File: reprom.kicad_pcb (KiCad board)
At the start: 2 copper layers, 54.4 x 40.6 mm, 20 parts, among them P1 KERNAL_SOCKET, P10 NEW_LEFT, P11 SX64_RIGHT, P12 ANCIENT_RIGHT, P13 GND, P2 KERNAL_AND_BASIC_SOCKET, P3 ANCIENT_LEFT, P4 OLD_RIGHT, P5 KERNAL, P6 CHARSET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

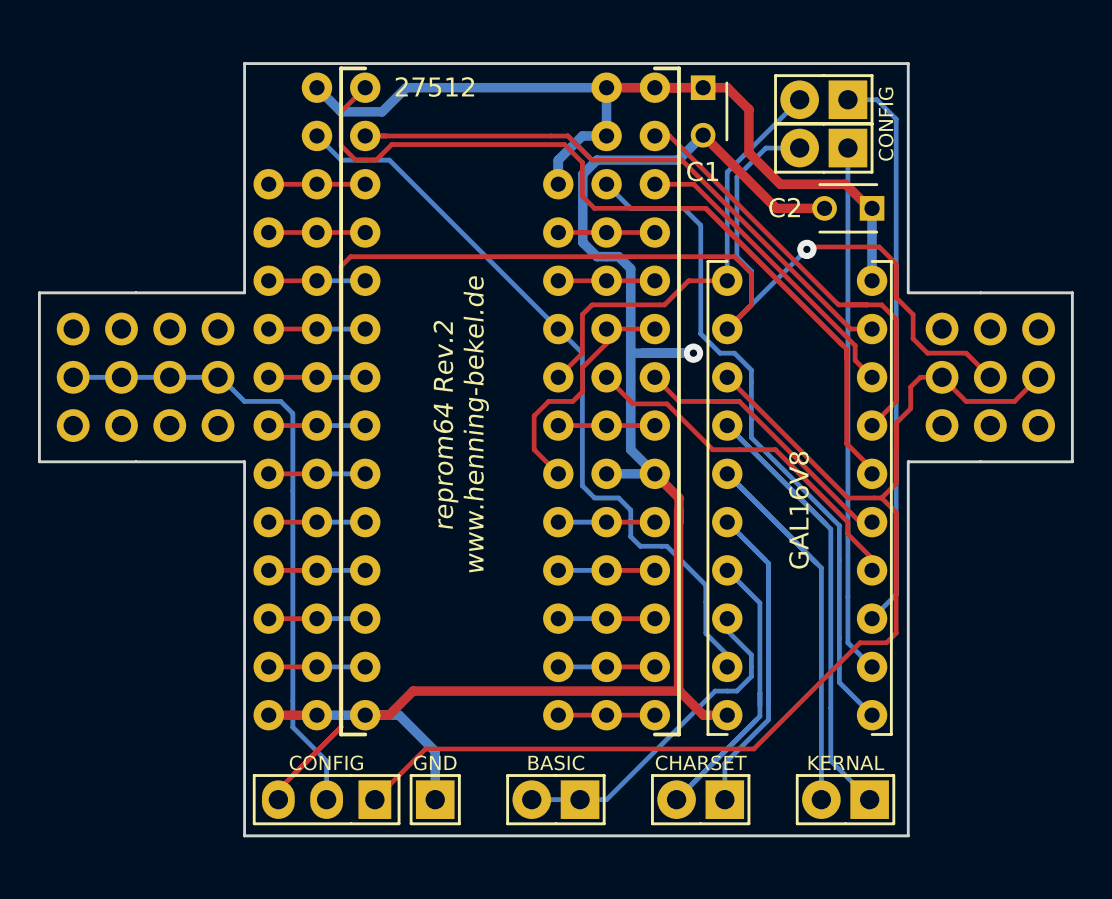
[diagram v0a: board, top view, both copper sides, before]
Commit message: Hardware: Added additional pin header for A5 and A8, rounded corners
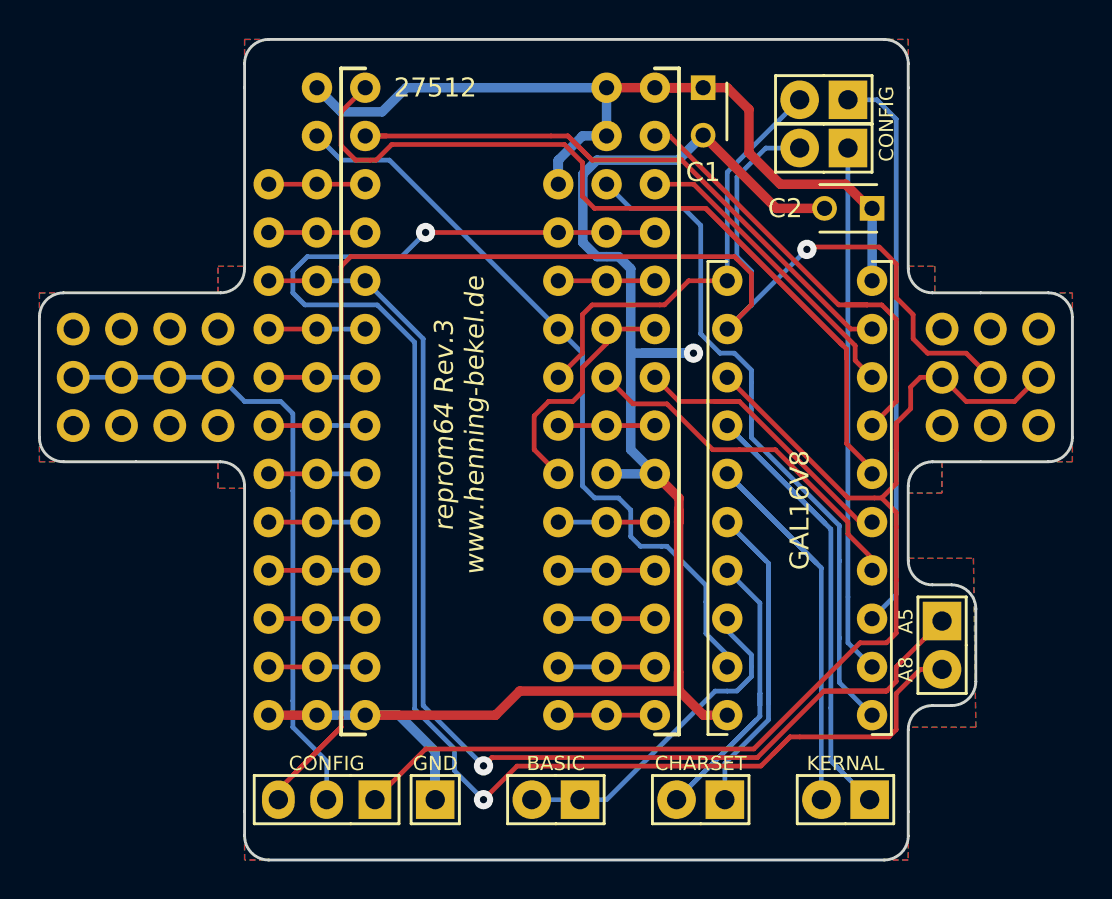
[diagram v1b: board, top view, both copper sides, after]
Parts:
- added P14: AUX, custom:Pin_Header_Straight_1x02, F.Cu at (158.8, 106.8)
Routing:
- net /A8: track 5.08 -> 83.4 mm, vias 0 -> 2
- net /A5: track 5.08 -> 64.2 mm, vias 0 -> 1
- net GND: track 86.5 -> 89.3 mm
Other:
- board size 54.4 x 40.6 mm -> 54.4 x 43.2 mm
- board text added: "A5"
- board text added: "A8"
- board text added: "reprom64 Rev.3 www.henning-bekel.de"
- board text removed: "reprom64 Rev.2 www.henning-bekel.de"

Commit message: Hardware: Moved A5 and A8 header to a more convenient location
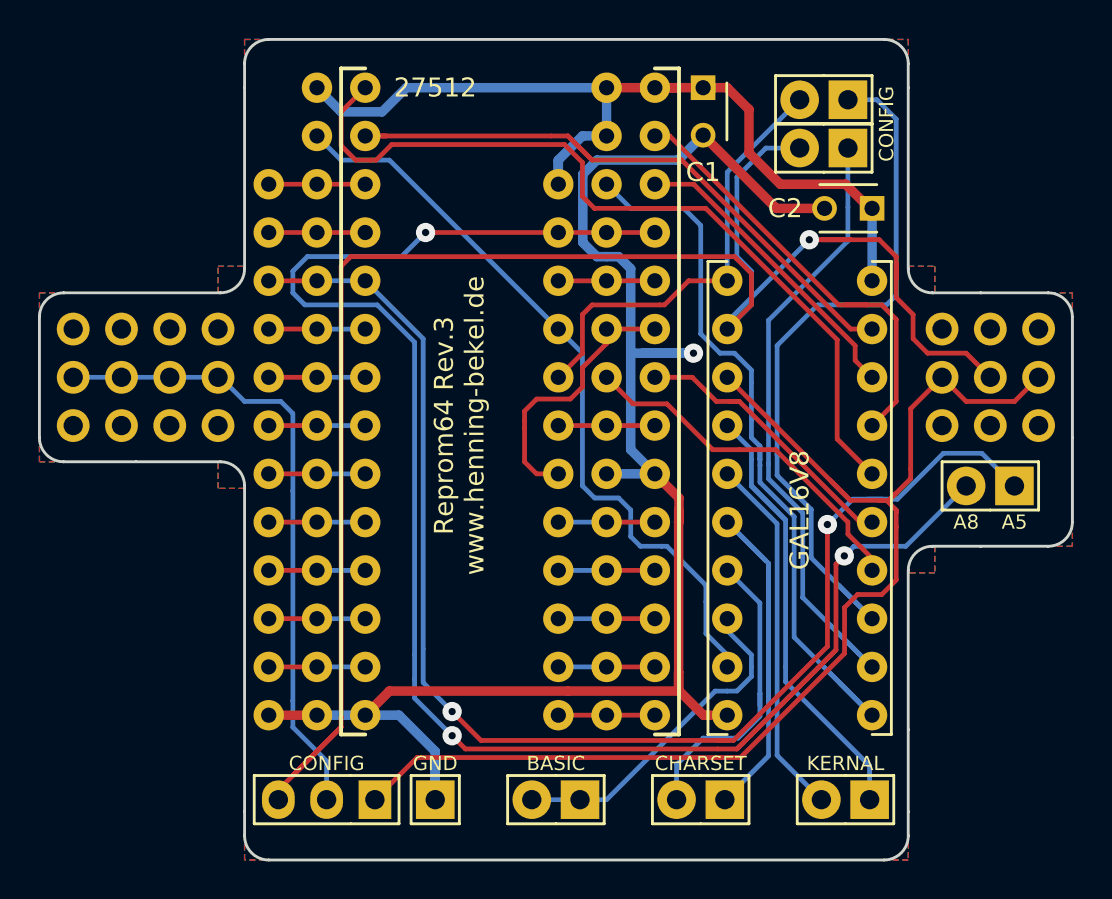
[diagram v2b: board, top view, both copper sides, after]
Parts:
- moved P14 8.07 mm to (162.6, 99.7), turned to 270 degrees
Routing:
- net /K1: track 31.2 -> 19.2 mm
- net /A15: track 54.1 -> 43.7 mm
- net /A8: track 83.4 -> 93.2 mm, vias 2 -> 3
- net /CKS: track 29.8 -> 38.5 mm
- net /A5: track 64.2 -> 72.0 mm, vias 1 -> 2
- net /BA14: track 35.8 -> 42.7 mm
- net /CBS: track 27.8 -> 34.4 mm
- net /C1: track 21.2 -> 16.3 mm
- net /K0: track 30.1 -> 25.4 mm
- net /BS: track 91.7 -> 95.0 mm
- net /A11: track 13.0 -> 14.4 mm
- net /OE: track 16.0 -> 15.2 mm
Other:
- outline, holes or cut-outs redrawn
- board text added: "Reprom64 Rev.3 www.henning-bekel.de"
- board text removed: "reprom64 Rev.3 www.henning-bekel.de"

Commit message: Hardware: Improved silkscreen, routing
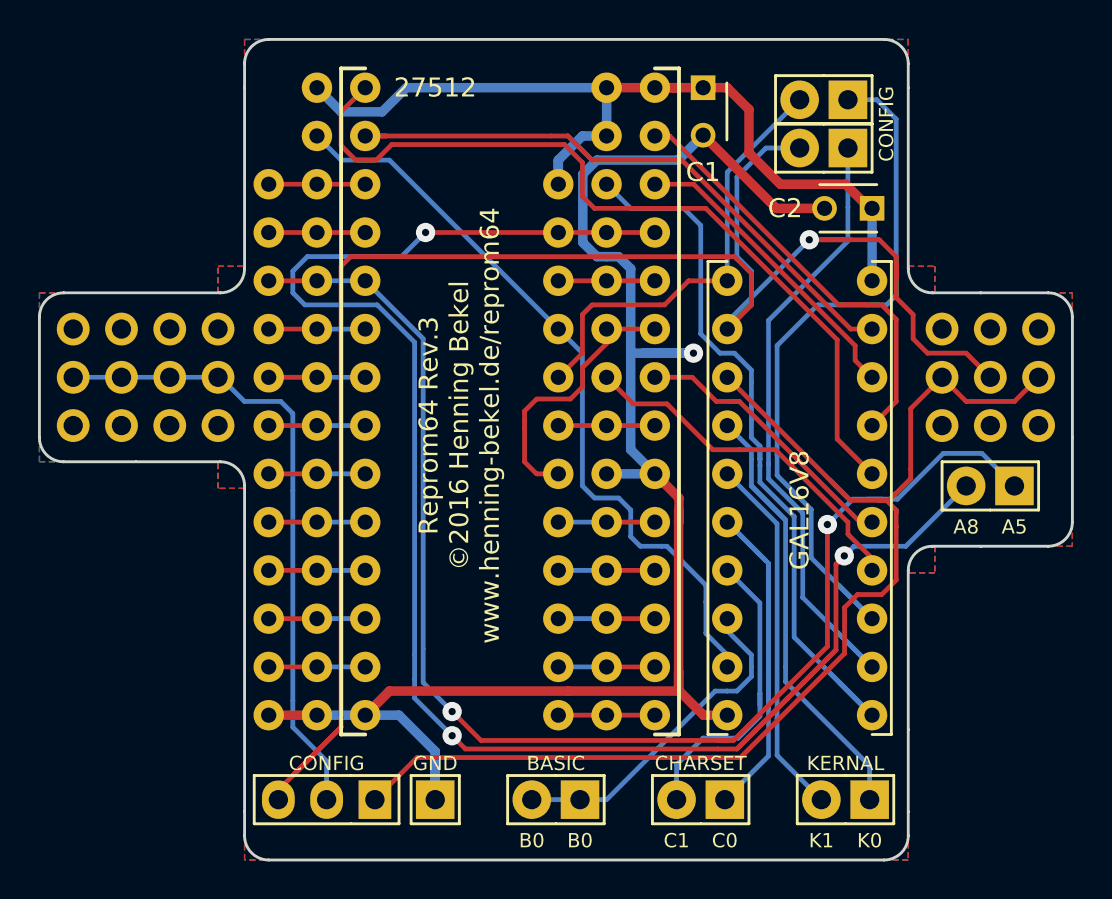
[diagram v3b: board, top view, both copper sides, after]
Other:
- board text added: "B0"
- board text added: "C0"
- board text added: "C1"
- board text added: "K0"
- board text added: "K1"
- board text added: "Reprom64 Rev.3 ©2016 Henning Bekel www.henning-bekel.de/reprom64"
- board text removed: "Reprom64 Rev.3 www.henning-bekel.de"
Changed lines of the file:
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@@
     (area 111.176999 76.124999 165.683001 119.455001)
     (thickness 1.6)
-    (drawings 50)
+    (drawings 56)
     (tracks 387)
     (zones 0)
@@
     (pad 2 thru_hole oval (at 0 2.54 270) (size 2.032 2.032) (drill 1.016) (layers *.Cu *.Mask F.SilkS)
       (net 24 /A8))
-    (model Pin_Headers.3dshapes/Pin_Header_Angled_1x02.wrl
-      (at (xyz 0 -0.05 0))
-      (scale (xyz 1 1 1))
-      (rotate (xyz 0 0 90))
-    )
+  )
+  (gr_text K0 (at 154.94 118.364) (layer F.SilkS)
+    (effects (font (size 0.75 0.75) (thickness 0.15)))
+  )
+  (gr_text K1 (at 152.4 118.364) (layer F.SilkS)
+    (effects (font (size 0.75 0.75) (thickness 0.15)))
+  )
+  (gr_text C0 (at 147.32 118.364) (layer F.SilkS)
+    (effects (font (size 0.75 0.75) (thickness 0.15)))
+  )
+  (gr_text C1 (at 144.78 118.364) (layer F.SilkS)
+    (effects (font (size 0.75 0.75) (thickness 0.15)))
+  )
+  (gr_text B0 (at 139.7 118.364) (layer F.SilkS)
+    (effects (font (size 0.75 0.75) (thickness 0.15)))
+  )
+  (gr_text B0 (at 137.16 118.364) (layer F.SilkS)
+    (effects (font (size 0.75 0.75) (thickness 0.15)))
   )
   (gr_line (start 156.972 112.522) (end 156.972 104.14) (angle 90) (layer Edge.Cuts) (width 0.15))
@@
   (gr_line (start 156.972 78.74) (end 156.972 77.47) (angle 90) (layer Edge.Cuts) (width 0.15))
   (gr_line (start 122.047 78.74) (end 122.047 77.47) (angle 90) (layer Edge.Cuts) (width 0.15))
-  (gr_text A8 (at 160.02 101.6) (layer F.SilkS)
-    (effects (font (size 0.75 0.75) (thickness 0.15)))
-  )
-  (gr_text A5 (at 162.56 101.6) (layer F.SilkS)
+  (gr_text A8 (at 160.02 101.854) (layer F.SilkS)
+    (effects (font (size 0.75 0.75) (thickness 0.15)))
+  )
+  (gr_text A5 (at 162.56 101.854) (layer F.SilkS)
     (effects (font (size 0.75 0.75) (thickness 0.15)))
   )
@@
     (effects (font (size 0.75 0.75) (thickness 0.15)))
   )
-  (gr_text "Reprom64 Rev.3\nwww.henning-bekel.de" (at 133.35 96.52 90) (layer F.SilkS)
+  (gr_text "Reprom64 Rev.3\n©2016 Henning Bekel\nwww.henning-bekel.de/reprom64" (at 133.35 96.52 90) (layer F.SilkS)
     (effects (font (size 1 1) (thickness 0.15)))
   )
@@
   (segment (start 152.908 99.441) (end 147.447 93.98) (width 0.25) (layer F.Cu) (net 29))
   (segment (start 147.447 94.105602) (end 147.447 93.98) (width 0.25) (layer F.Cu) (net 29))
-  (segment (start 154.94 116.205) (end 154.94 114.427) (width 0.25) (layer B.Cu) (net 31) (status 400000))
+  (segment (start 154.94 116.205) (end 154.94 114.427) (width 0.25) (layer B.Cu) (net 31))
   (segment (start 150.517008 110.004008) (end 150.517008 109.22) (width 0.25) (layer B.Cu) (net 31))
   (segment (start 154.94 114.427) (end 150.517008 110.004008) (width 0.25) (layer B.Cu) (net 31))

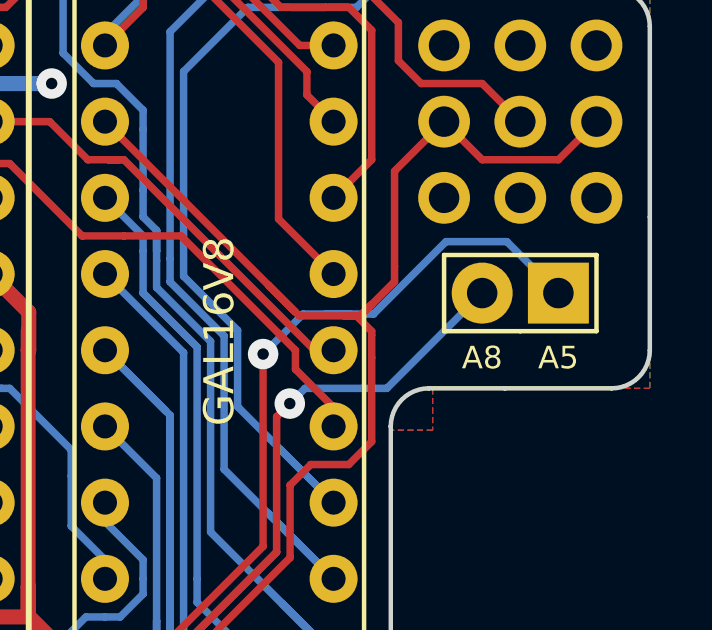
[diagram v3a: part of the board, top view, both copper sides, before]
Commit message: Hardware: Reversed order of A5 and A8
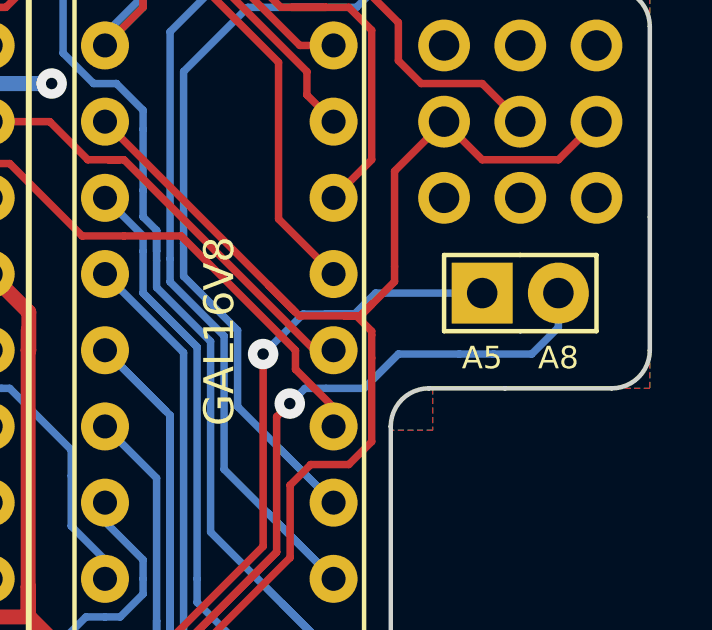
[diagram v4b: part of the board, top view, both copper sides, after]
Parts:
- moved P14 2.54 mm to (160.0, 99.7), turned to 90 degrees
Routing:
- net /A5: track 72.0 -> 68.0 mm
- net /A8: track 93.2 -> 96.4 mm
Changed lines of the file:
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@@
     (thickness 1.6)
     (drawings 56)
-    (tracks 387)
+    (tracks 392)
     (zones 0)
     (modules 21)
@@
   )
   (module custom:Pin_Header_Straight_1x02 (layer F.Cu)
-    (at 162.56 99.695 270)
-    (descr "Through hole pin header")
-    (tags "pin header")
-    (fp_text reference P14 (at 5.715 1.27 360) (layer F.SilkS) hide
-      (effects (font (size 1 1) (thickness 0.15)))
-    )
-    (fp_text value AUX (at 4.445 1.27 360) (layer F.Fab)
+    (at 160.02 99.695 90)
+    (descr "Through hole pin header")
+    (tags "pin header")
+    (fp_text reference P14 (at 5.715 1.27 180) (layer F.SilkS) hide
+      (effects (font (size 1 1) (thickness 0.15)))
+    )
+    (fp_text value AUX (at 4.445 1.27 180) (layer F.Fab)
       (effects (font (size 1 1) (thickness 0.15)))
     )
@@
     (fp_line (start -1.27 1.27) (end -1.27 3.81) (layer F.SilkS) (width 0.15))
     (fp_line (start -1.27 3.81) (end 1.27 3.81) (layer F.SilkS) (width 0.15))
-    (pad 1 thru_hole rect (at 0 0 270) (size 2.032 2.032) (drill 1.016) (layers *.Cu *.Mask F.SilkS)
+    (pad 1 thru_hole rect (at 0 0 90) (size 2.032 2.032) (drill 1.016) (layers *.Cu *.Mask F.SilkS)
       (net 5 /A5))
-    (pad 2 thru_hole oval (at 0 2.54 270) (size 2.032 2.032) (drill 1.016) (layers *.Cu *.Mask F.SilkS)
+    (pad 2 thru_hole oval (at 0 2.54 90) (size 2.032 2.032) (drill 1.016) (layers *.Cu *.Mask F.SilkS)
       (net 24 /A8))
   )
@@
   (gr_line (start 156.972 78.74) (end 156.972 77.47) (angle 90) (layer Edge.Cuts) (width 0.15))
   (gr_line (start 122.047 78.74) (end 122.047 77.47) (angle 90) (layer Edge.Cuts) (width 0.15))
-  (gr_text A8 (at 160.02 101.854) (layer F.SilkS)
-    (effects (font (size 0.75 0.75) (thickness 0.15)))
-  )
-  (gr_text A5 (at 162.56 101.854) (layer F.SilkS)
+  (gr_text A5 (at 160.02 101.854) (layer F.SilkS)
+    (effects (font (size 0.75 0.75) (thickness 0.15)))
+  )
+  (gr_text A8 (at 162.56 101.854) (layer F.SilkS)
     (effects (font (size 0.75 0.75) (thickness 0.15)))
   )
@@
   (segment (start 128.397 86.36) (end 125.857 86.36) (width 0.25) (layer F.Cu) (net 4))
   (segment (start 125.857 86.36) (end 123.317 86.36) (width 0.25) (layer F.Cu) (net 4))
-  (segment (start 154.813 100.3935) (end 156.4005 100.3935) (width 0.25) (layer B.Cu) (net 5))
-  (segment (start 160.8455 97.9805) (end 162.56 99.695) (width 0.25) (layer B.Cu) (net 5))
-  (segment (start 158.8135 97.9805) (end 160.8455 97.9805) (width 0.25) (layer B.Cu) (net 5))
-  (segment (start 156.4005 100.3935) (end 158.8135 97.9805) (width 0.25) (layer B.Cu) (net 5))
+  (segment (start 160.02 99.695) (end 156.464 99.695) (width 0.25) (layer B.Cu) (net 5))
+  (segment (start 156.464 99.695) (end 155.7655 100.3935) (width 0.25) (layer B.Cu) (net 5))
+  (segment (start 155.7655 100.3935) (end 154.813 100.3935) (width 0.25) (layer B.Cu) (net 5))
   (segment (start 146.939 113.087998) (end 147.770002 113.087998) (width 0.25) (layer F.Cu) (net 5))
+  (segment (start 147.770002 113.087998) (end 152.7175 108.1405) (width 0.25) (layer F.Cu) (net 5))
+  (segment (start 152.7175 108.1405) (end 152.7175 101.727) (width 0.25) (layer F.Cu) (net 5))
+  (via (at 152.7175 101.727) (size 1.016) (drill 0.381) (layers F.Cu B.Cu) (net 5))
+  (segment (start 152.7175 101.727) (end 154.051 100.3935) (width 0.25) (layer B.Cu) (net 5))
   (segment (start 154.051 100.3935) (end 154.813 100.3935) (width 0.25) (layer B.Cu) (net 5))
   (segment (start 154.813 100.3935) (end 155.6385 100.3935) (width 0.25) (layer B.Cu) (net 5))
-  (segment (start 152.7175 101.727) (end 154.051 100.3935) (width 0.25) (layer B.Cu) (net 5))
-  (via (at 152.7175 101.727) (size 1.016) (drill 0.381) (layers F.Cu B.Cu) (net 5))
-  (segment (start 152.7175 108.1405) (end 152.7175 101.727) (width 0.25) (layer F.Cu) (net 5))
-  (segment (start 147.770002 113.087998) (end 152.7175 108.1405) (width 0.25) (layer F.Cu) (net 5))
   (segment (start 131.445 108.2675) (end 131.445 110.0455) (width 0.25) (layer B.Cu) (net 5))
   (segment (start 134.487498 113.087998) (end 146.939 113.087998) (width 0.25) (layer F.Cu) (net 5))
@@
   (segment (start 143.637 88.9) (end 141.097 88.9) (width 0.25) (layer F.Cu) (net 23))
   (segment (start 141.097 88.9) (end 138.557 88.9) (width 0.25) (layer F.Cu) (net 23))
+  (segment (start 160.401 101.727) (end 161.671 101.727) (width 0.25) (layer B.Cu) (net 24))
+  (segment (start 161.671 101.727) (end 162.56 100.838) (width 0.25) (layer B.Cu) (net 24))
+  (segment (start 159.258 101.727) (end 160.401 101.727) (width 0.25) (layer B.Cu) (net 24))
+  (segment (start 162.56 100.838) (end 162.56 99.695) (width 0.25) (layer B.Cu) (net 24) (status 800000))
+  (segment (start 154.813 102.87) (end 156.083 102.87) (width 0.25) (layer B.Cu) (net 24))
+  (segment (start 157.226 101.727) (end 159.258 101.727) (width 0.25) (layer B.Cu) (net 24))
+  (segment (start 156.083 102.87) (end 157.226 101.727) (width 0.25) (layer B.Cu) (net 24))
   (segment (start 146.939 113.538) (end 147.956398 113.538) (width 0.25) (layer F.Cu) (net 24))
   (segment (start 147.956398 113.538) (end 153.167502 108.326896) (width 0.25) (layer F.Cu) (net 24))
@@
   (segment (start 146.939 113.538) (end 133.6675 113.538) (width 0.25) (layer F.Cu) (net 24))
   (segment (start 153.167502 108.326896) (end 147.956398 113.538) (width 0.25) (layer F.Cu) (net 24))
-  (segment (start 156.845 102.87) (end 160.02 99.695) (width 0.25) (layer B.Cu) (net 24))
-  (segment (start 154.1145 102.87) (end 156.845 102.87) (width 0.25) (layer B.Cu) (net 24))
+  (segment (start 154.1145 102.87) (end 154.813 102.87) (width 0.25) (layer B.Cu) (net 24))
   (segment (start 153.6065 103.378) (end 154.1145 102.87) (width 0.25) (layer B.Cu) (net 24))
   (via (at 153.6065 103.378) (size 1.016) (drill 0.381) (layers F.Cu B.Cu) (net 24))
